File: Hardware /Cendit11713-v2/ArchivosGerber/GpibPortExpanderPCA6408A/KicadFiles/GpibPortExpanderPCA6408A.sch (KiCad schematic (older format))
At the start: 26 parts, among them P1 CONN_01X07, U1 PCA6408A, U2 PCA6408A

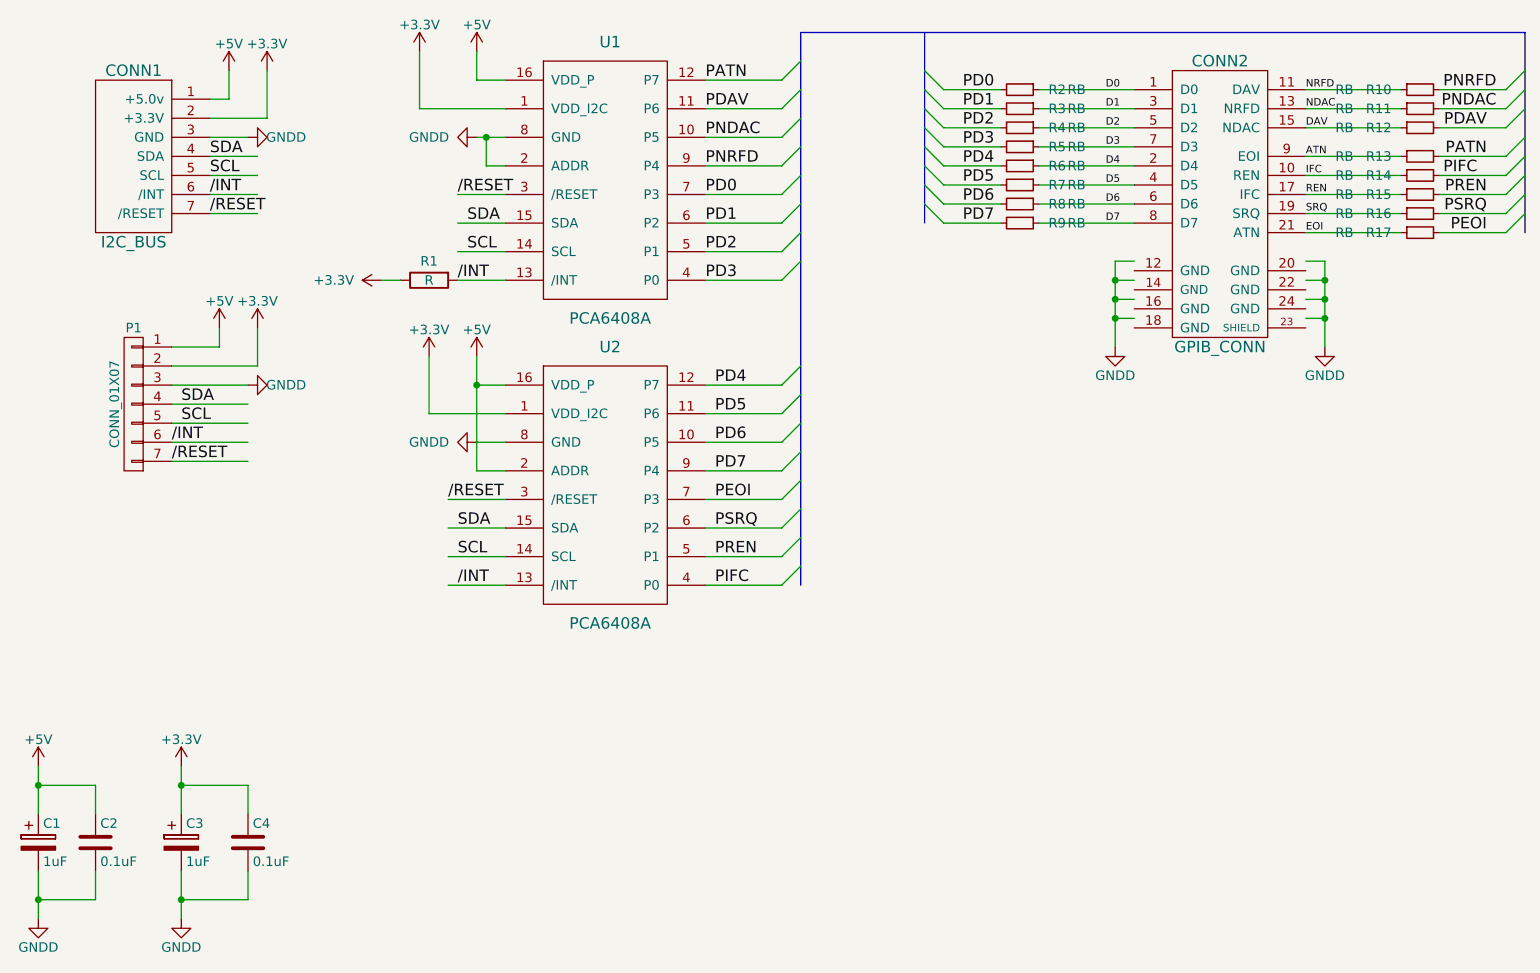
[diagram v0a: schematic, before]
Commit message: En Cendit11713 + respaldo de software
  - Esquematico tarjeta madre con PIC18F45K50
  - Respaldo de software CenditLab
  - Gerber files tarjeta interfaz GPIB
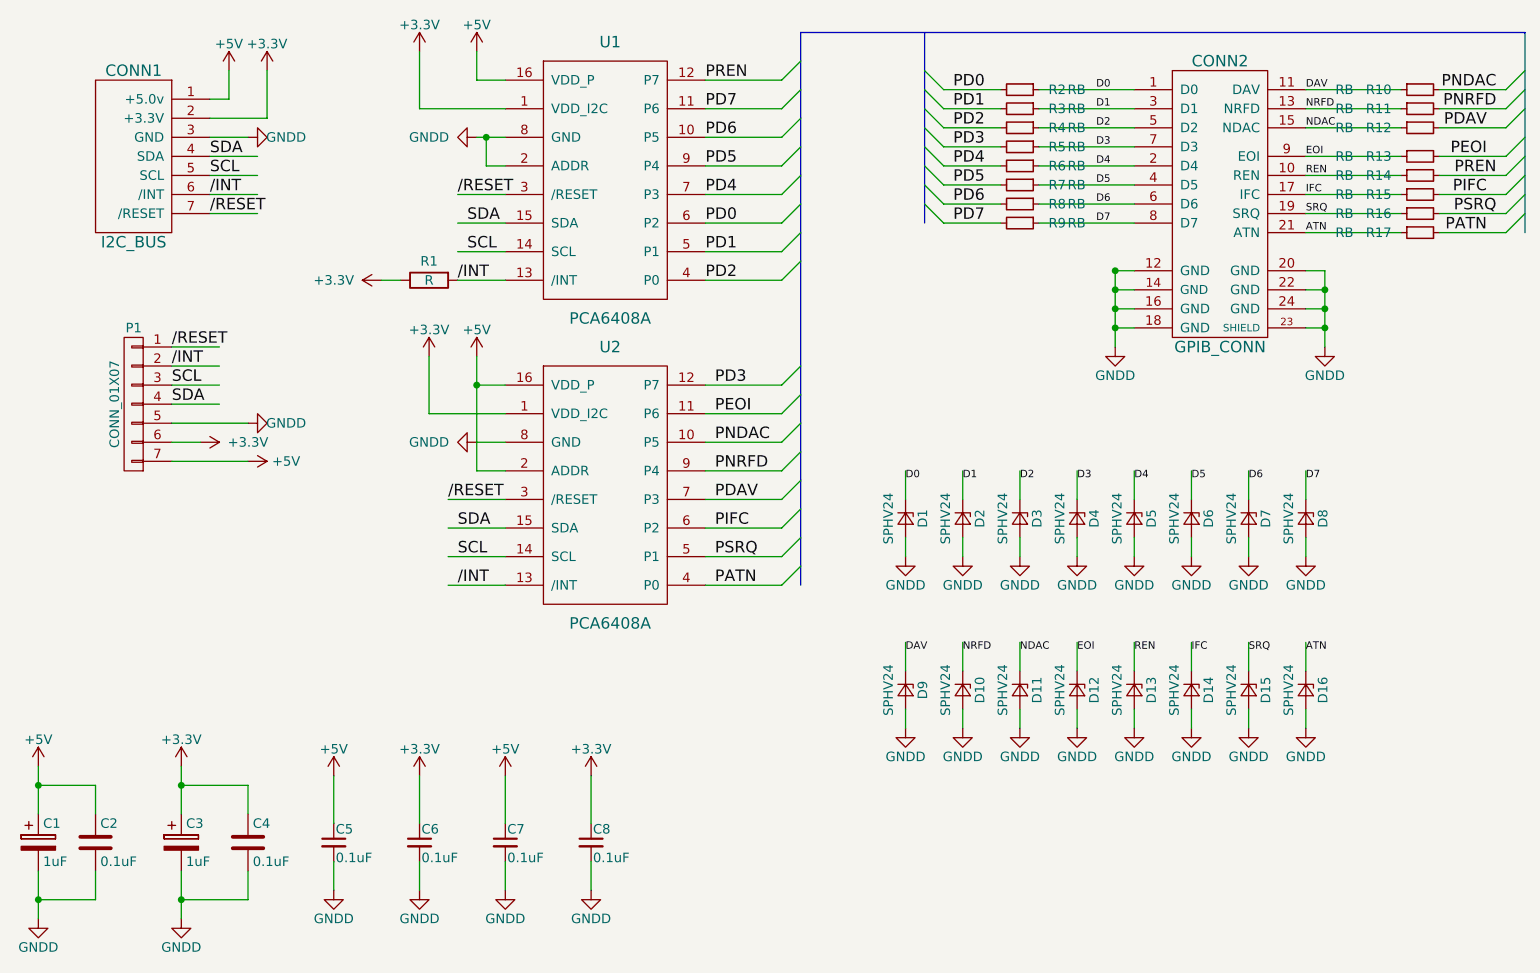
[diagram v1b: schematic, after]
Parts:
- added C5, C6, C7, C8: 0.1uF, Capacitors_SMD:C_0805_HandSoldering, symbol C_Small
- added D1, D10, D11, D12, D13, D14, D15, D16, D2, D3, D4, D5, D6, D7, D8, D9: SPHV24, CenditFootprints:SPHV24-SOD882, symbol D_Zener_Small
- CONN2: footprint CenditFootprints:GPIB_HEADER_12X2P -> (none)
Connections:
- wire segments 110 -> 148

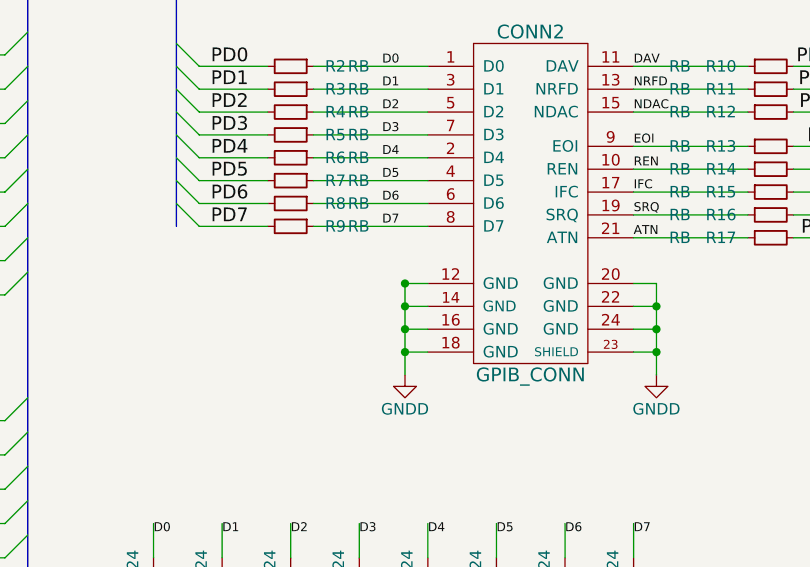
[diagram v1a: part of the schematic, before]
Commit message: En Cendit11713 + CenditLab respaldo
  - Se revisan tarjetas
  - Correccion en PCB GPIB
  - Se inicia tarjeta madre en una pieza (MainBoard.OnePiece)
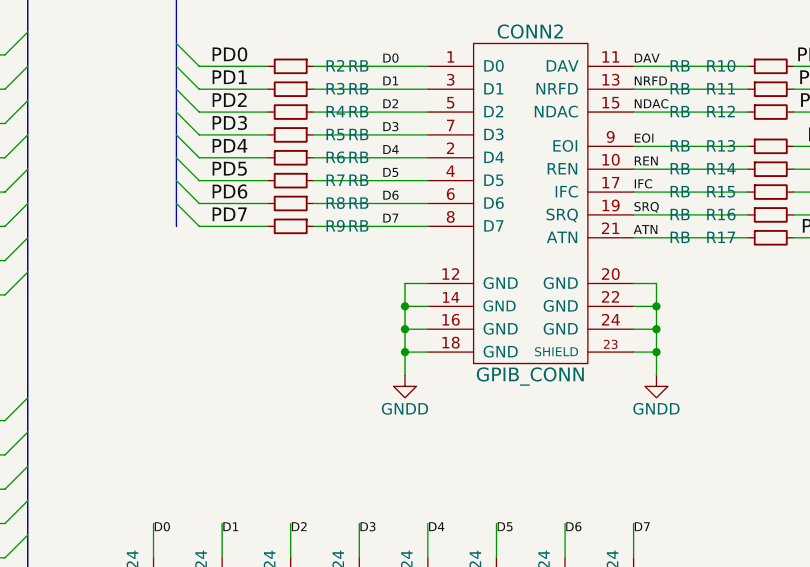
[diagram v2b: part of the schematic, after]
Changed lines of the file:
@@
 EELAYER 25 0
 EELAYER END
-$Descr A4 11693 8268
+$Descr USLetter 11000 8500
 encoding utf-8
 Sheet 1 1
-Title ""
-Date ""
-Rev ""
-Comp ""
-Comment1 ""
-Comment2 ""
-Comment3 ""
+Title "Tarjeta para interfaz con bus GPIB"
+Date "2017-11-28"
+Rev "1.0"
+Comp "CENDIT"
+Comment1 "Basada en IC PCA6408, expansor de puertos serial SPI a paralelo"
+Comment2 "correo@josearias.com.ve"
+Comment3 "Jose Arias"
 Comment4 ""
 $EndDescr
@@
 Wire Wire Line
 	6750 3050 6650 3050
-Connection ~ 6650 3050
 Wire Wire Line
 	1700 3550 1950 3550
